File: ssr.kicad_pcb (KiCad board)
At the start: 2 copper layers, 99.1 x 76.2 mm, 39 parts, among them IC1 ATTINY44-SS, P2 CONTACT, P4 CONTACT, P5 CONTACT, Q1 MOSFET_N, U1 MOC-3052, U2 TRIAC, U3 LTV-814

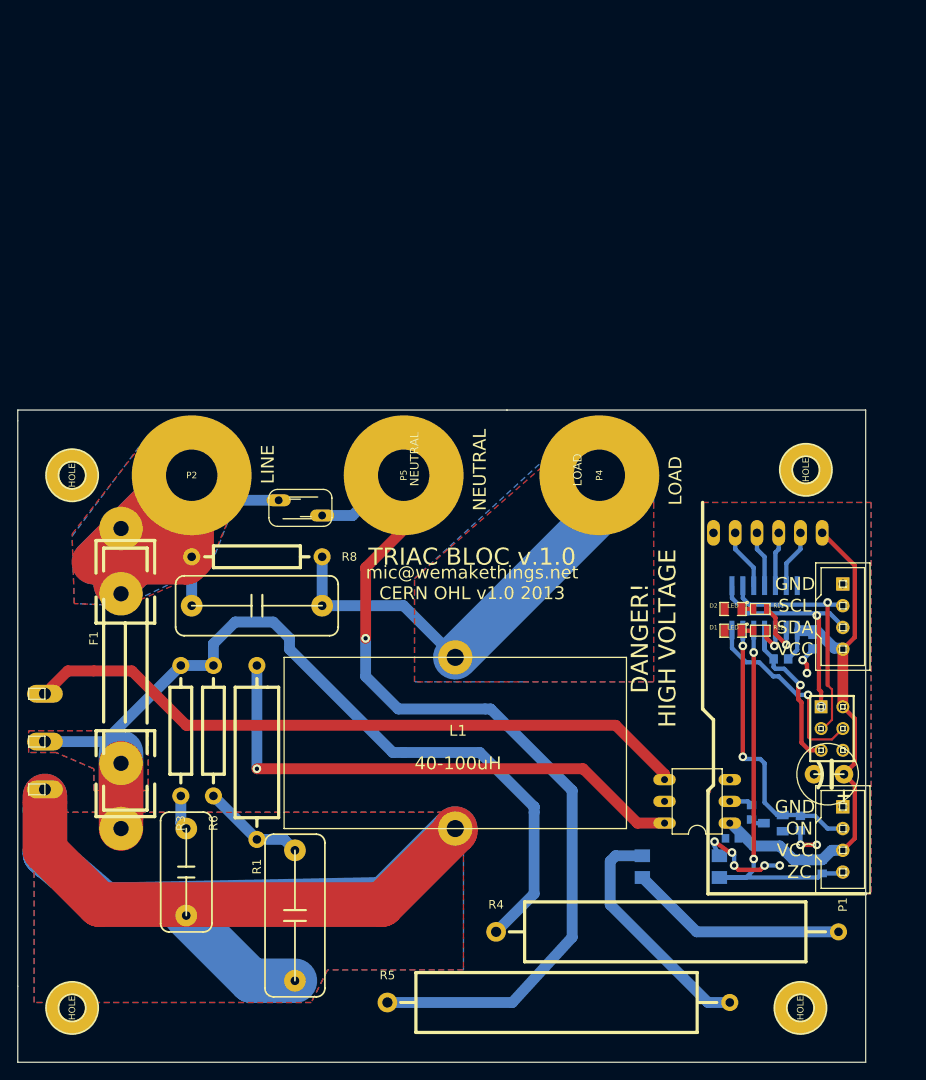
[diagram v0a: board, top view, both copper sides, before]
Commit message: some work on firmware, experiments, some documentation has been added
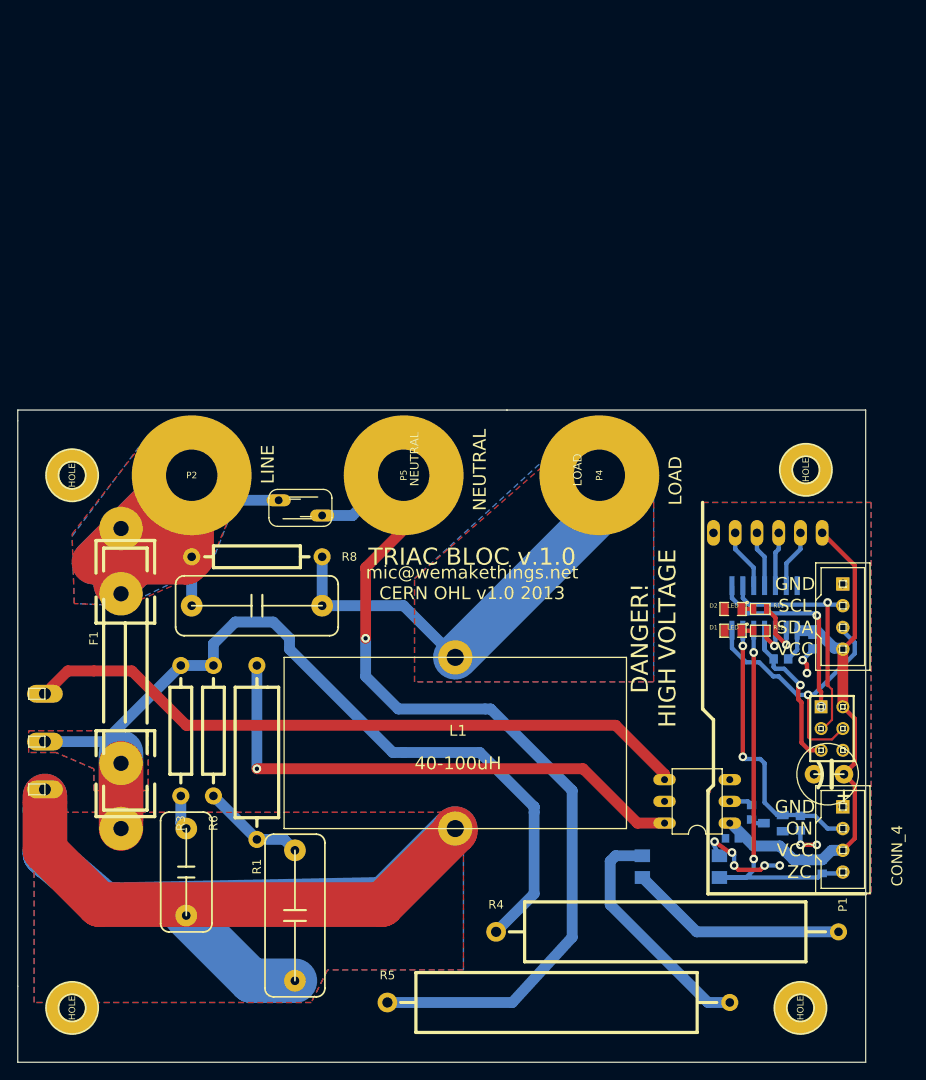
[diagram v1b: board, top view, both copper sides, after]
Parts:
- C5: value (none) -> 100uF
- P1, P6: value (none) -> CONN_4
- R10: value (none) -> R
- R2: value (none) -> 200R
- R9: value (none) -> 10k
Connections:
- P6 pad 3: /MISO -> /MOSI
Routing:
- net N-000008: track 140.1 -> 166.5 mm
- net /MOSI: track 22.9 -> 34.0 mm
- net /MISO: track 26.9 -> 23.2 mm

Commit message: Change MCU to attiny441, add rs485, change board dimensions to half-euro-pannel, change leds to THT, change connectors, total reroute
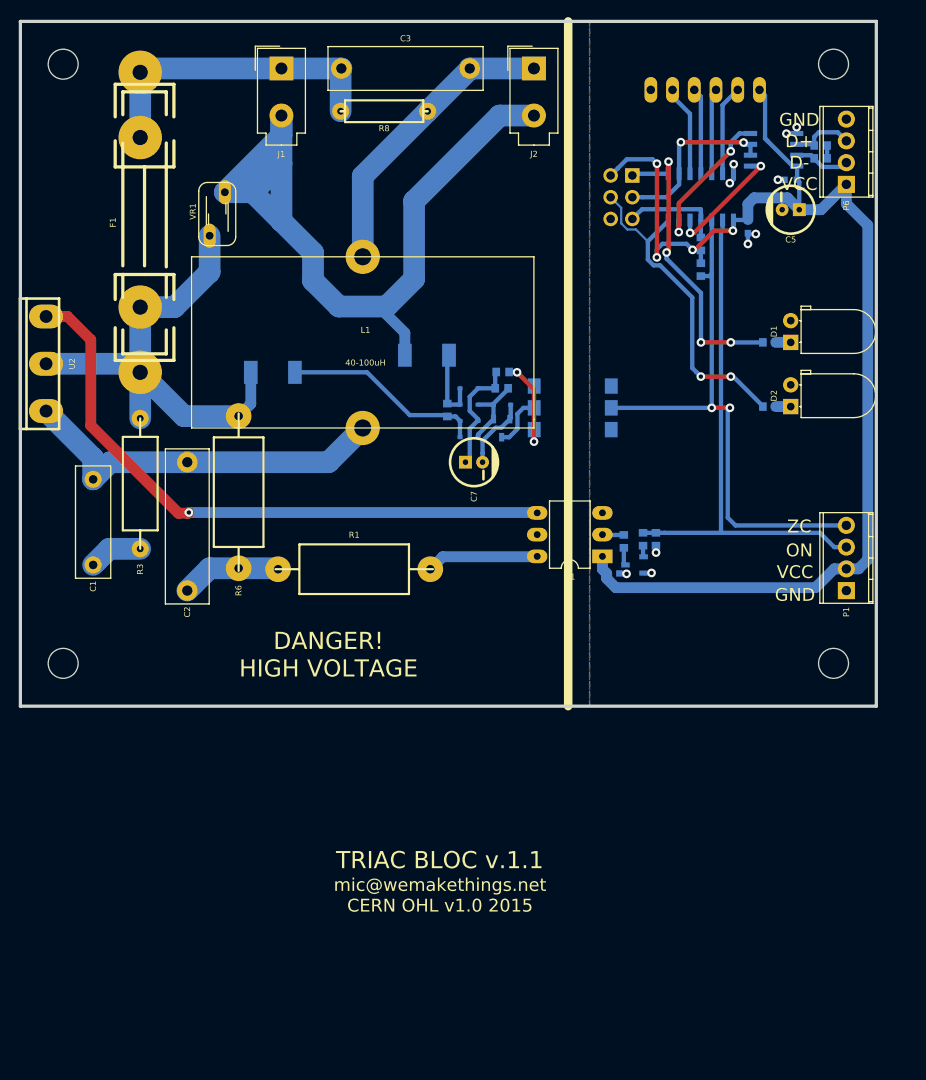
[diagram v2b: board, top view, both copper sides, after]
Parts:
- removed ?: ISP, atmel-AVR-ISP-6
- removed HOLE (x4): Val**, HOLE_30
- removed IC1: ATTINY44-SS, -SO-14
- removed P2, P4, P5: CONTACT, HOLE_60
- added C7: 10u, w_capacitors:CP_5x11mm, F.Cu at (153.0, 71.5)
- added C8: 1n, w_smd_cap:c_0603, B.Cu at (149.9, 65.4)
- added C9: 1u, Capacitors_SMD:C_0603, B.Cu at (190.0, 38.5)
- added CON1: AVR-ISP-6, Pin_Headers:Pin_Header_Straight_2x03_Pitch2.54mm, B.Cu at (171.5, 38.0)
- added D3: 1N4148, Diodes_SMD:D_SOD-323, B.Cu at (156.2, 64.8)
- added D4: 1N4148, Diodes_SMD:D_SOD-323, B.Cu at (152.4, 66.7)
- added D5: 1N4148, Diodes_SMD:D_SOD-323, B.Cu at (152.4, 62.9)
- added D6: 1N4148, Diodes_SMD:D_SOD-323, B.Cu at (152.4, 64.8)
- added D7: 1N4148, Diodes_SMD:D_SOD-323, B.Cu at (152.4, 68.6)
- added IC2: ATTINY441-SSU, Housings_SOIC:SOIC-14_3.9x8.7mm_Pitch1.27mm, B.Cu at (179.5, 40.5)
- added J1: 240VAC, Connectors_Molex:Molex_MiniFit-JR-5556-02A_2x01x4.20mm_Straight, F.Cu at (130.5, 25.5)
- added J2: LOAD, Connectors_Molex:Molex_MiniFit-JR-5556-02A_2x01x4.20mm_Straight, F.Cu at (160.0, 25.5)
- added Q2: 2N3904, w_smd_trans:sot23, B.Cu at (156.2, 67.5)
- added R13: 220k, w_smd_resistors:r_2010, B.Cu at (129.5, 61.0)
- added R14: 220k, w_smd_resistors:r_2010, B.Cu at (147.5, 59.0)
- added R15: 1k, w_smd_resistors:r_0603, B.Cu at (172.8, 80.5)
- added R16: 0R, w_smd_resistors:r_0603, B.Cu at (193.5, 34.5)
- added R17: 120, w_smd_resistors:r_0603, B.Cu at (193.5, 36.0)
- added REF**: EuroBoard_halb_Type-I_100mmX80mm_holes, EuroBoard_Outline:EuroBoard_halb_Type-I_100mmX80mm_holes, F.Cu at (100.0, 100.0)
- added U4: SP3485EN, Housings_SOIC:SOIC-8_3.9x4.9mm_Pitch1.27mm, B.Cu at (188.0, 35.0)
- C1: footprint rc-master-C100-140X060 -> Capacitors_ThroughHole:C_Rect_L13.0mm_W4.0mm_P10.00mm_FKS3_FKP3_MKS4
- C2, C3: footprint rc-master-C150-190X070 -> Capacitors_ThroughHole:C_Rect_L18.0mm_W5.0mm_P15.00mm_FKS3_FKP3
- C4: value 100nF -> 1u; footprint -C0603 -> Capacitors_SMD:C_0603
- C5: footprint rc-master-CE-035X100 -> w_capacitors:CP_5x11mm
- C6: footprint c_0603 -> Capacitors_SMD:C_0603
- CONN10: renamed from ?; value (none) -> CONN_01X06
- D1, D2: footprint SM0805 -> LEDs:LED_D5.0mm_Horizontal_O1.27mm_Z3.0mm
- P1, P6: footprint connect-SC-04 -> Connectors_Terminal_Blocks:TerminalBlock_Pheonix_MPT-2.54mm_4pol
- Q1: value MOSFET_N -> 2N3904; footprint -SOT23 -> w_smd_trans:sot23
- R1: footprint Resistor_Horizontal_RM20mm -> w_pth_resistors:R12x5.2
- R10: value R -> 200; footprint -R0603 -> w_smd_resistors:r_0603
- R11, R12: value R -> 220; footprint SM0603 -> w_smd_resistors:r_0603; moved to B.Cu
- R2: value 200R -> 4.7k; footprint rc-master-R0603 -> w_smd_resistors:r_0603
- R3: footprint Resistor_Horizontal_RM15mm -> w_pth_resistors:RC07
- R4: value 8.2k 5W -> 1k; footprint Resistor_Horizontal_RM30mm -> w_smd_resistors:r_0603; moved to B.Cu
- R5: value 8.2k 5W -> 22k; footprint Resistor_Horizontal_RM30mm -> w_smd_resistors:r_0603; moved to B.Cu
- R6: footprint Resistor_Horizontal_RM15mm -> w_pth_resistors:R12x5.2
- R7: value R -> 10k; footprint -R0603 -> w_smd_resistors:r_0603
- R8: footprint Resistor_Horizontal_RM15mm -> w_pth_resistors:RC05
- R9: footprint -R0603 -> w_smd_resistors:r_0603
- U1: footprint optocoupler-2-DIL06 -> Housings_DIP:DIP-6_W7.62mm_LongPads
- U2: value TRIAC -> BTA41; footprint -TOP3 -> w_to:top3
- U3: value LTV-814 -> 4N35; footprint optocoupler-2-SO-4 -> w_smd_dil:mdip_6
- moved R5 76.5 mm to (156.2, 62.9), turned to 0 degrees
- moved R4 76.3 mm to (156.3, 61.0), turned to 0 degrees
- moved R2 71.2 mm to (179.5, 49.0), turned to 270 degrees
- moved C5 66.1 mm to (190.0, 42.0), turned to 90 degrees
- moved C3 63.5 mm to (137.5, 25.5)
- moved R8 56.7 mm to (142.5, 30.5)
- moved U3 55.1 mm to (164.5, 65.2), turned to 90 degrees
- moved F1 53.3 mm to (114.0, 61.0)
- moved CONN10 52.3 mm to (180.0, 28.0)
- moved P6 50.5 mm to (196.5, 39.0), turned to 90 degrees
- moved R7 49.4 mm to (179.5, 46.0), turned to 90 degrees
- moved C4 49.0 mm to (185.0, 44.0)
- moved L1 48.0 mm to (120.0, 67.5)
- moved U2 44.8 mm to (103.0, 60.0)
- moved C2 40.0 mm to (119.5, 86.5), turned to 90 degrees
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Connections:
- net N-000001 renamed /FIRE
- net N-0000016 renamed /LOAD-FILTERED
- net N-000008 renamed /LOAD
- C3 pad 1: N-0000021 -> Net-(C3-Pad1)
- P1 pad 2: ON -> VCC
- P1 pad 3: VCC -> ON
- P6 pad 1: GND -> VCC
- P6 pad 2: /SCK -> /RS485-B
- P6 pad 3: /MOSI -> /RS485-A
- P6 pad 4: VCC -> GND
- R10 pad 2: N-0000019 -> Net-(Q1-Pad2)
- R11 pad 1: N-0000011 -> /MOSI
- R12 pad 1: N-0000013 -> /MISO
- R4 pad 2: /LINE -> Net-(C7-Pad1)
- R5 pad 1: N-000004 -> Net-(D3-Pad1)
- R5 pad 2: /NEUTRAL -> Net-(C7-Pad1)
- R8 pad 1: N-0000021 -> Net-(C3-Pad1)
- U3 pad 2: N-000004 -> Net-(Q2-Pad2)
- U3 pad 3: GND -> Net-(U3-Pad3)
- U3 pad 4: ZERO_CROSSING -> GND
- VR1 pad 1: N-0000021 -> /LINE
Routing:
- net /LOAD: track 166.5 -> 44.2 mm
- net N-0000021: track 102.7 -> 0.00 mm
- net VCC: track 69.9 -> 146.2 mm, vias 0 -> 4
- net Net-(R1-Pad1): track 62.3 -> 13.2 mm, vias 1 -> 0
- net /LINE: track 105.8 -> 58.4 mm
- net Net-(C3-Pad1): track 0.00 -> 36.3 mm
- net ON: track 32.6 -> 61.2 mm, vias 2 -> 0
- net N-000004: track 27.8 -> 0.00 mm
- net Net-(C8-Pad1): track 0.00 -> 24.1 mm
- net /LOAD-FILTERED: track 53.3 -> 34.7 mm
- net /TX: track 0.00 -> 17.2 mm, vias 0 -> 2
- net ZERO_CROSSING: track 47.8 -> 64.4 mm
- net /NEUTRAL: track 109.1 -> 93.5 mm, vias 1 -> 0
- net Net-(R4-Pad1): track 25.5 -> 11.3 mm, vias 0 -> 2
- net /RX: track 0.00 -> 14.2 mm, vias 0 -> 2
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- removed copper zone on B.Cu, net /LINE
- removed copper zone on F.Cu, net /LINE
- removed copper zone on B.Cu, net /LOAD
- removed copper zone on F.Cu, net /LOAD
- removed copper zone on B.Cu, net /LOAD-FILTERED
- removed copper zone on F.Cu, net /LOAD-FILTERED
- removed copper zone on B.Cu, net N-0000021
- removed copper zone on F.Cu, net N-0000021
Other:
- board size 99.1 x 76.2 mm -> 100 x 80 mm
- net class Default: clearance 0.254 -> 0
- rule trace_clearance: 0.254 -> 0
- rule trace_min: 0.254 -> 0.2
- board text added: "D+"
- board text added: "D-"
- board text added: "TRIAC BLOC v.1.1"
- board text added: "mic@wemakethings.net CERN OHL v1.0 2015"
- board text removed: "LINE"
- board text removed: "LOAD"
- board text removed: "NEUTRAL"
- board text removed: "SCL"
- board text removed: "SDA"
- board text removed: "TRIAC BLOC v.1.0"
- board text removed: "mic@wemakethings.net CERN OHL v1.0 2013"

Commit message: Shuffle silkscreen around, order the boards made
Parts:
- added REF***: OSHW-Logo2_9.8x8mm_SilkScreen, Symbols:OSHW-Logo2_9.8x8mm_SilkScreen, F.Cu at (183.0, 60.5)
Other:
- board text added: "AC IN ~~240V"
- board text added: "LOAD 2kW max"
- board text added: "TRIAC BLOC v.1.2"
- board text added: "mic@wemakethings.net github.com/Miceuz/triac-bloc CERN OHL v1.0 2017"
- board text removed: "TRIAC BLOC v.1.1"
- board text removed: "mic@wemakethings.net CERN OHL v1.0 2015"

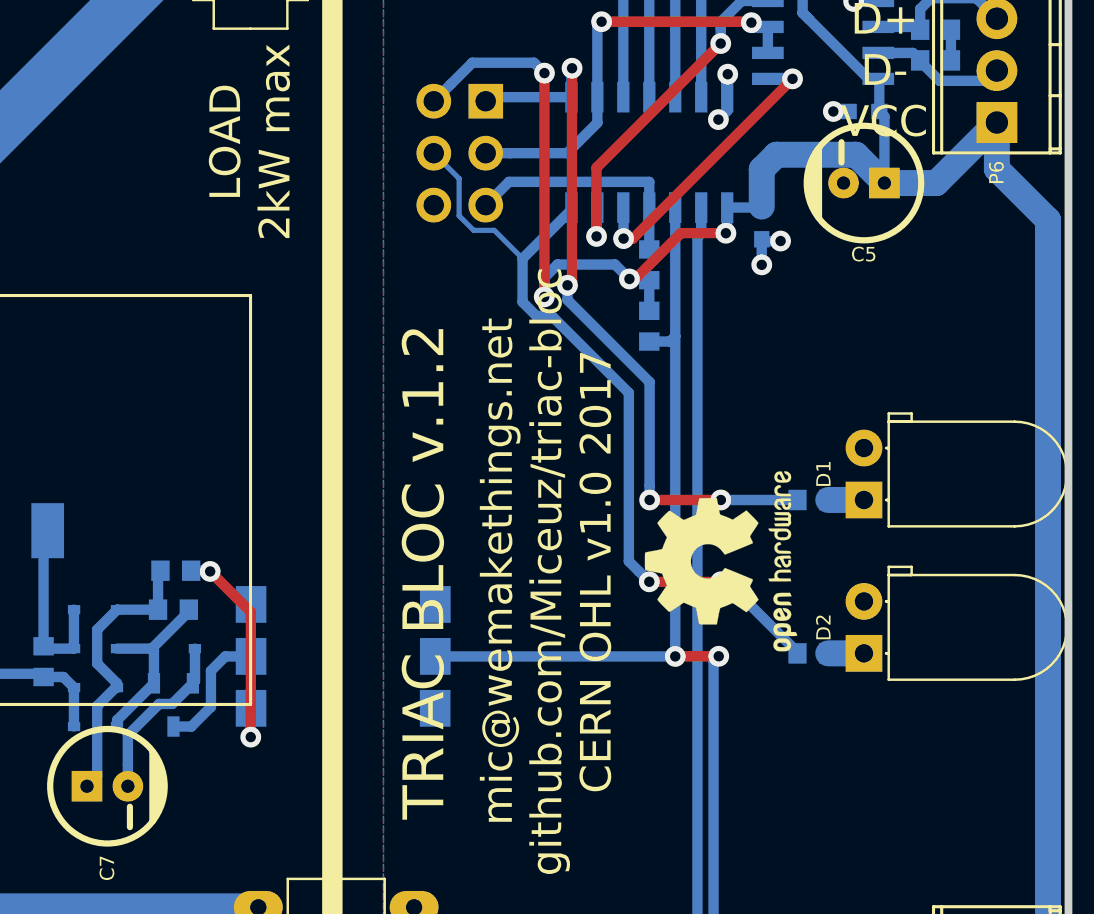
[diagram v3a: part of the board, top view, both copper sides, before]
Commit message: KiCad library change, export PDF schematics
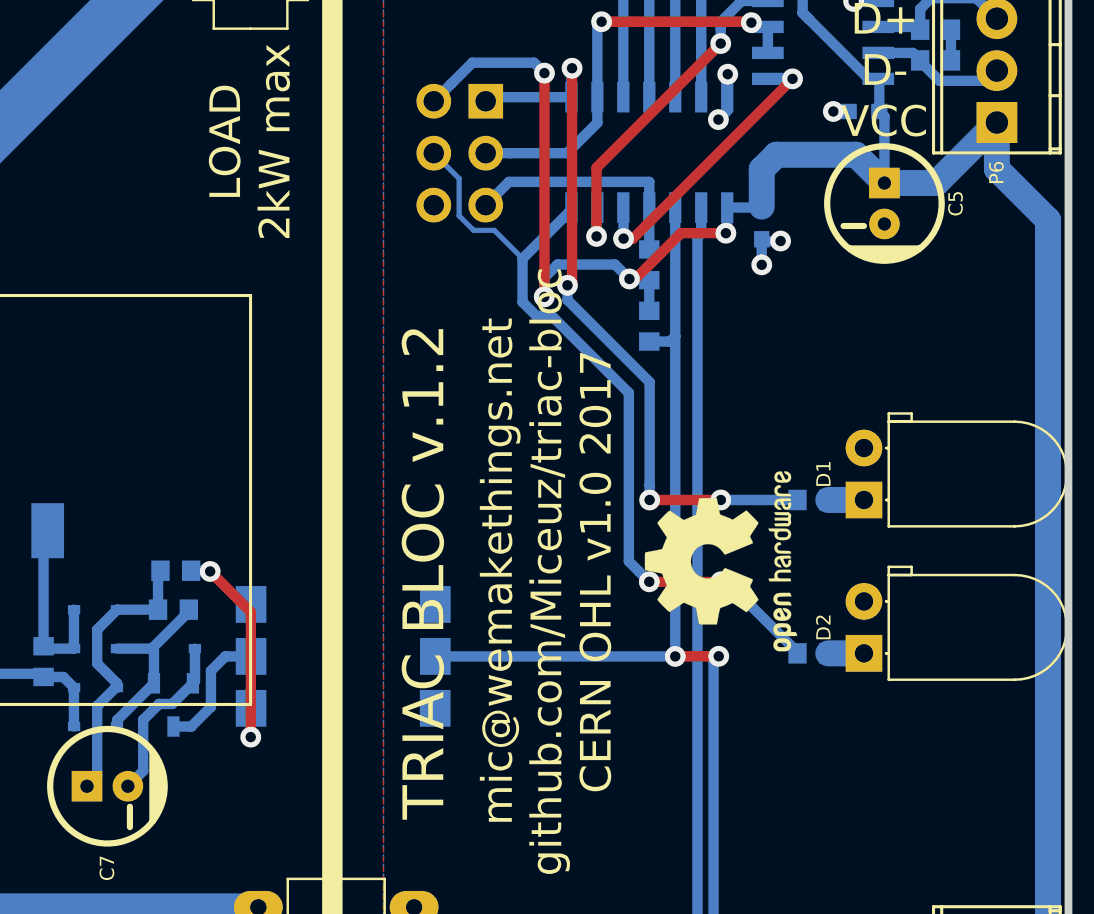
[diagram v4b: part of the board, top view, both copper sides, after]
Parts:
- moved C5 1.41 mm to (191.0, 43.0), turned to 180 degrees
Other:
- net class Default: clearance 0 -> 0.1
- rule trace_clearance: 0 -> 0.1
